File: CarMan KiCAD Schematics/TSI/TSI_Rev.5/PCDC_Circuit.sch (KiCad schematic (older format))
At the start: 57 parts, among them IC1 TS431ILT, J30 GLV Hook-up Pin, K1 APAN3105, Q1 ZVP1320F, Q3 SI1302DL-T1-E3, U10 MC7805BDTRKG, U12 REF3033, U19 SN74HC00APWR, U21 MCP6004, U27 TLP293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

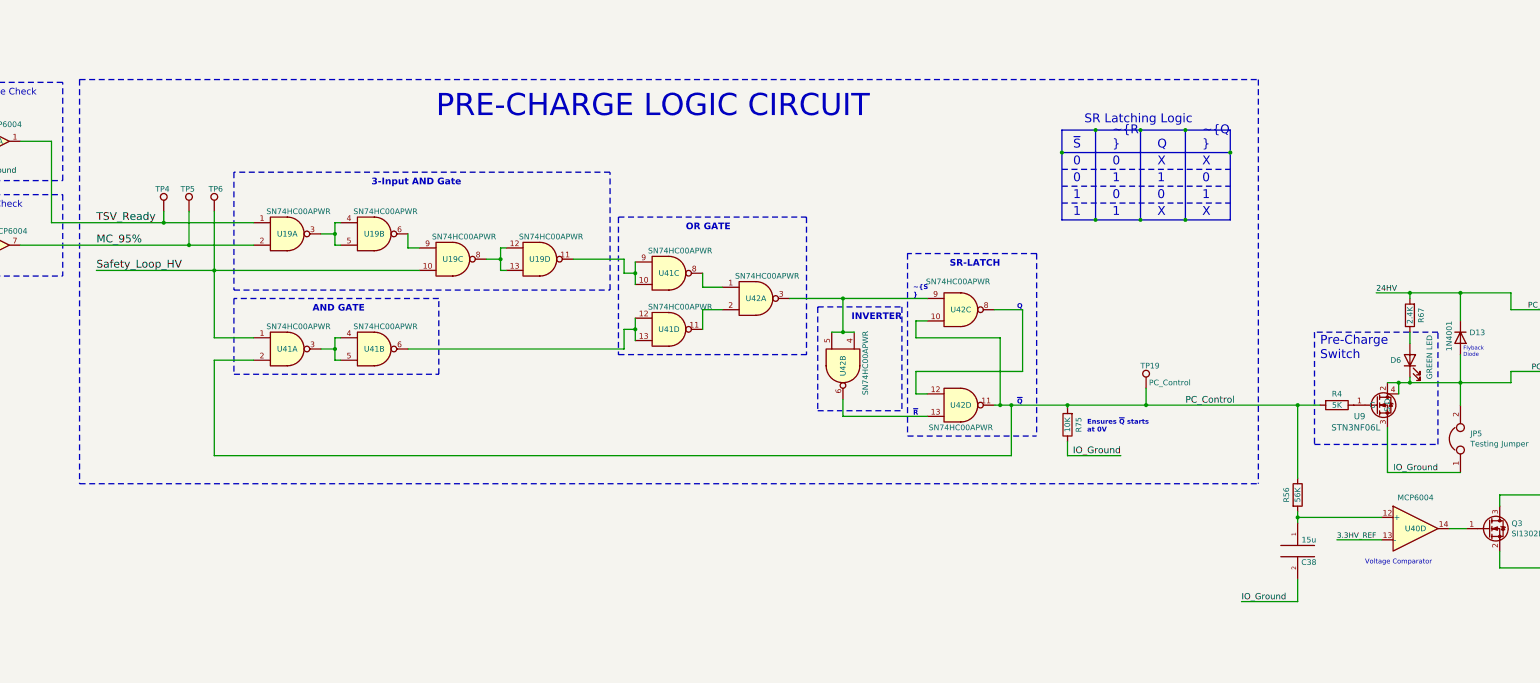
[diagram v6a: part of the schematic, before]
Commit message: Changed D6, Pre-Charge LED to a better circuit, wasn't working before. floating voltage at gate of Xsistor U9 was turning it on always
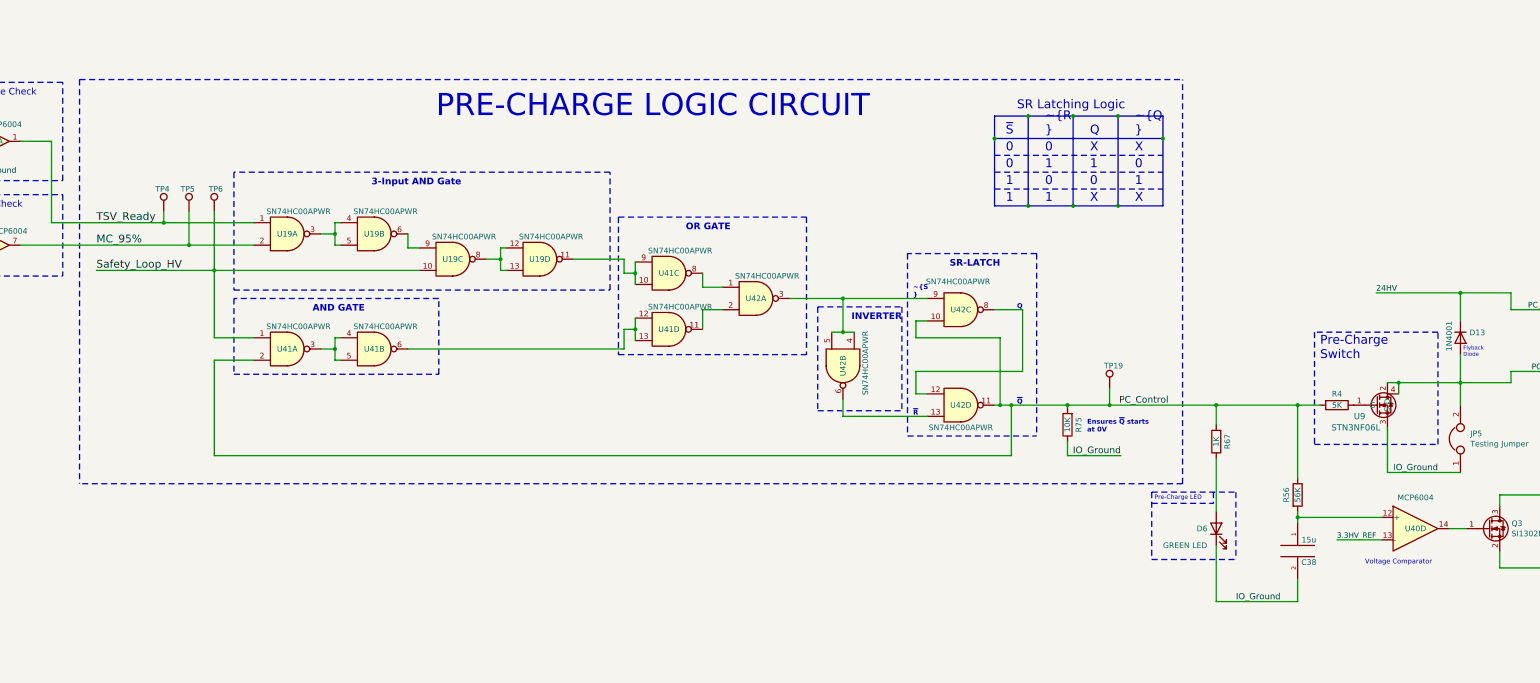
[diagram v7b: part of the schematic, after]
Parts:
- R67: value 2.4K -> 1K
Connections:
- net DC_RELAY-: now also D6.1 (K)
- net PC_Control: now also R67.2
- net PC_RELAY+: no longer R67.2
- net PC_RELAY-: no longer D6.1 (K)
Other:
- note added: "Pre-Charge LED"
- moved on the sheet: D6, R67, TP19
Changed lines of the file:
@@
 Wire Wire Line
 	17050 6425 17050 6625
-Connection ~ 16600 6425
-Wire Wire Line
-	16600 6425 16500 6425
-Wire Wire Line
-	16600 5625 16600 5675
-Wire Wire Line
-	16600 5975 16600 6075
-Wire Wire Line
-	16600 6425 16600 6375
-Wire Wire Line
-	16300 5625 16600 5625
 Text Label 16850 7225 2    55   ~ 0
 IO_Ground
-Connection ~ 16600 5625
 Wire Wire Line
 	16400 7225 17050 7225
@@
 Wire Wire Line
 	17050 5625 17050 5875
-Wire Wire Line
-	16600 6425 17050 6425
-Wire Wire Line
-	16600 5625 17050 5625
 $Comp
 L Device:D D13
@@
 PRE-CHARGE LOGIC CIRCUIT
 Wire Notes Line
-	4750 3725 4750 7325
-Wire Notes Line
 	18075 3600 22100 3600
 Wire Notes Line
@@
 	1    0    0    -1
 $EndComp
-Text Label 15100 8375 0    55   ~ 0
+Text Label 15050 8375 0    55   ~ 0
 IO_Ground
-Wire Wire Line
-	15100 8375 15600 8375
 $Comp
 L Device:LED D6
 U 1 1 5F9CE834
-P 16600 6225
-F 0 "D6" V 16600 6400 50  0000 R CNN
-F 1 "GREEN LED" H 16825 6050 50  0000 R CNN
-F 2 "LED_SMD:LED_0805_2012Metric_Pad1.15x1.40mm_HandSolder" H 16600 6225 50  0001 C CNN
-F 3 "http://static.vcclite.com/pdf/VAOL-S8GT4-LED-0805-green.pdf" H 16600 6225 50  0001 C CNN
-F 4 "VAOL-S8GT4" V 16600 6225 50  0001 C CNN "Part Name"
-	1    16600 6225
+P 14875 7725
+F 0 "D6" V 14875 7900 50  0000 R CNN
+F 1 "GREEN LED" V 14725 8200 50  0000 R CNN
+F 2 "LED_SMD:LED_0805_2012Metric_Pad1.15x1.40mm_HandSolder" H 14875 7725 50  0001 C CNN
+F 3 "http://static.vcclite.com/pdf/VAOL-S8GT4-LED-0805-green.pdf" H 14875 7725 50  0001 C CNN
+F 4 "VAOL-S8GT4" V 14875 7725 50  0001 C CNN "Part Name"
+	1    14875 7725
 	0    -1   -1   0
 $EndComp
-Wire Notes Line
-	4750 3725 15250 3725
-Wire Notes Line
-	4750 7325 15250 7325
-Text Label 14600 6625 0    59   ~ 0
+Text Label 14450 6625 2    59   ~ 0
 PC_Control
-Connection ~ 14250 6625
-Wire Wire Line
-	14250 6625 15600 6625
-Wire Wire Line
-	13550 6625 14250 6625
+Wire Wire Line
+	13550 6625 13925 6625
 $Comp
 L Connector:TestPoint TP?
 U 1 1 60D4CBAD
-P 14250 6475
+P 13925 6475
 AR Path="/5FC85F57/60D4CBAD" Ref="TP?"  Part="1"
 AR Path="/6196BF15/60D4CBAD" Ref="TP19"  Part="1"
-F 0 "TP19" H 14200 6675 50  0000 L CNN
-F 1 "PC_Control" H 14275 6525 50  0000 L CNN
-F 2 "TestPoint:TestPoint_Pad_D3.0mm" H 14450 6475 50  0001 C CNN
-F 3 "~" H 14450 6475 50  0001 C CNN
-	1    14250 6475
-	1    0    0    -1
-$EndComp
-Wire Wire Line
-	14250 6475 14250 6625
-Wire Notes Line
-	15250 3725 15250 7325
-Wire Bus Line
-	15000 4175 15000 4375
-Wire Bus Line
-	13500 4175 13500 4375
-Wire Bus Line
-	15000 4375 15000 4975
-Connection ~ 15000 4375
-Wire Bus Line
-	13500 4375 13500 4975
-Connection ~ 13500 4375
-Text Notes 14750 4650 0    79   ~ 0
+F 0 "TP19" H 13875 6675 50  0000 L CNN
+F 1 "PC_Control" H 13950 6525 50  0001 L CNN
+F 2 "TestPoint:TestPoint_Pad_D3.0mm" H 14125 6475 50  0001 C CNN
+F 3 "~" H 14125 6475 50  0001 C CNN
+	1    13925 6475
+	1    0    0    -1
+$EndComp
+Wire Wire Line
+	13925 6475 13925 6625
+Wire Bus Line
+	14400 4050 14400 4250
+Wire Bus Line
+	12900 4050 12900 4250
+Wire Bus Line
+	14400 4250 14400 4850
+Connection ~ 14400 4250
+Wire Bus Line
+	12900 4250 12900 4850
+Connection ~ 12900 4250
+Text Notes 14150 4525 0    79   ~ 0
 0\n
-Text Notes 14350 4950 0    79   ~ 0
+Text Notes 13750 4825 0    79   ~ 0
 X
-Text Notes 14425 4500 2    79   ~ 0
+Text Notes 13825 4375 2    79   ~ 0
 X
 Wire Notes Line
-	13500 4825 15000 4825
-Wire Notes Line
-	13500 4675 15000 4675
-Wire Notes Line
-	13500 4525 15000 4525
-Wire Bus Line
-	15000 4375 13500 4375
-Wire Bus Line
-	14600 4975 15000 4975
-Wire Bus Line
-	14600 4175 14600 4975
-Connection ~ 14600 4975
-Connection ~ 14600 4175
-Text Notes 14750 4500 0    79   ~ 0
+	12900 4700 14400 4700
+Wire Notes Line
+	12900 4550 14400 4550
+Wire Notes Line
+	12900 4400 14400 4400
+Wire Bus Line
+	14400 4250 12900 4250
+Wire Bus Line
+	14000 4850 14400 4850
+Wire Bus Line
+	14000 4050 14000 4850
+Connection ~ 14000 4850
+Connection ~ 14000 4050
+Text Notes 14150 4375 0    79   ~ 0
 X
-Text Notes 14750 4950 0    79   ~ 0
+Text Notes 14150 4825 0    79   ~ 0
 X
-Text Notes 14750 4800 0    79   ~ 0
+Text Notes 14150 4675 0    79   ~ 0
 1
 Wire Bus Line
-	15000 4175 14600 4175
-Text Notes 14750 4350 0    79   ~ 0
+	14400 4050 14000 4050
+Text Notes 14150 4225 0    79   ~ 0
 ~Q\n
-Text Notes 13700 4125 0    79   ~ 0
+Text Notes 13100 4000 0    79   ~ 0
 SR Latching Logic\n
 Wire Bus Line
-	14200 4975 14600 4975
-Wire Bus Line
-	14200 4175 14200 4975
-Connection ~ 14200 4975
-Text Notes 14350 4800 0    79   ~ 0
+	13600 4850 14000 4850
+Wire Bus Line
+	13600 4050 13600 4850
+Connection ~ 13600 4850
+Text Notes 13750 4675 0    79   ~ 0
 0
-Text Notes 14350 4650 0    79   ~ 0
+Text Notes 13750 4525 0    79   ~ 0
 1\n
-Text Notes 13950 4650 0    79   ~ 0
+Text Notes 13350 4525 0    79   ~ 0
 1\n
-Text Notes 13600 4950 0    79   ~ 0
+Text Notes 13000 4825 0    79   ~ 0
 1\n
-Text Notes 13600 4800 0    79   ~ 0
+Text Notes 13000 4675 0    79   ~ 0
 1\n
-Text Notes 13950 4950 0    79   ~ 0
+Text Notes 13350 4825 0    79   ~ 0
 1\n
-Text Notes 13950 4500 0    79   ~ 0
+Text Notes 13350 4375 0    79   ~ 0
 0
-Text Notes 13950 4800 0    79   ~ 0
+Text Notes 13350 4675 0    79   ~ 0
 0
-Text Notes 13600 4650 0    79   ~ 0
+Text Notes 13000 4525 0    79   ~ 0
 0
-Text Notes 13600 4500 0    79   ~ 0
+Text Notes 13000 4375 0    79   ~ 0
 0
 Wire Bus Line
-	14200 4175 13800 4175
-Connection ~ 14200 4175
-Wire Bus Line
-	13800 4975 14200 4975
-Connection ~ 13800 4975
-Wire Bus Line
-	13800 4175 13500 4175
-Connection ~ 13800 4175
-Wire Bus Line
-	13800 4175 13800 4975
-Wire Bus Line
-	13500 4975 13800 4975
-Wire Bus Line
-	14600 4175 14200 4175
-Text Notes 14350 4350 0    79   ~ 0
+	13600 4050 13200 4050
+Connection ~ 13600 4050
+Wire Bus Line
+	13200 4850 13600 4850
+Connection ~ 13200 4850
+Wire Bus Line
+	13200 4050 12900 4050
+Connection ~ 13200 4050
+Wire Bus Line
+	13200 4050 13200 4850
+Wire Bus Line
+	12900 4850 13200 4850
+Wire Bus Line
+	14000 4050 13600 4050
+Text Notes 13750 4225 0    79   ~ 0
 Q\n
-Text Notes 13950 4350 0    79   ~ 0
+Text Notes 13350 4225 0    79   ~ 0
 ~R\n
-Text Notes 13600 4350 0    79   ~ 0
+Text Notes 13000 4225 0    79   ~ 0
 ~S
 $Comp
 L Device:R R67
 U 1 1 5F9DBFC0
-P 16600 5825
-F 0 "R67" V 16500 5825 50  0000 C CNN
-F 1 "2.4K" V 16600 5825 50  0000 C CNN
-F 2 "Resistor_SMD:R_0805_2012Metric_Pad1.15x1.40mm_HandSolder" V 16530 5825 50  0001 C CNN
-F 3 "~" H 16600 5825 50  0001 C CNN
-	1    16600 5825
+P 14875 6950
+F 0 "R67" V 14775 6950 50  0000 C CNN
+F 1 "1K" V 14875 6950 50  0000 C CNN
+F 2 "Resistor_SMD:R_0805_2012Metric_Pad1.15x1.40mm_HandSolder" V 14805 6950 50  0001 C CNN
+F 3 "~" H 14875 6950 50  0001 C CNN
+	1    14875 6950
 	-1   0    0    1
 $EndComp
 Text Label 8720 12025 2    50   ~ 0
 IO_Ground
+Connection ~ 13925 6625
+Wire Wire Line
+	13925 6625 14875 6625
+Wire Notes Line
+	14575 7325 4750 7325
+Wire Notes Line
+	4750 3725 4750 7325
+Wire Wire Line
+	16300 5625 17050 5625
+Wire Wire Line
+	16500 6425 17050 6425
+Wire Wire Line
+	14875 6625 14875 6800
+Connection ~ 14875 6625
+Wire Wire Line
+	14875 6625 15600 6625
+Wire Wire Line
+	14875 8375 15600 8375
+Wire Wire Line
+	14875 7875 14875 8375
+Wire Wire Line
+	14875 7100 14875 7575
+Text Notes 14325 7475 0    39   ~ 0
+Pre-Charge LED
+Wire Notes Line
+	14300 7400 15050 7400
+Wire Notes Line
+	14850 7400 14850 7500
+Wire Notes Line
+	14575 7325 14575 3725
+Wire Notes Line
+	4750 3725 14575 3725
+Wire Notes Line
+	14300 7500 14850 7500
+Wire Notes Line
+	15050 7400 15050 8000
+Wire Notes Line
+	14300 8000 15050 8000
+Wire Notes Line
+	14300 7400 14300 8000
 $EndSCHEMATC

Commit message: changed the "speical" footprint of U9 to the correct one
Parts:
- U9: footprint TSI_Rev_2021_Footprint_Lib:SOT230P700X180-4N-speical -> TSI_Rev_2021_Footprint_Lib:SOT230P700X180-4N
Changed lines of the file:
@@
 F 0 "U9" H 16100 6525 55  0000 L CNN
 F 1 "STN3NF06L" H 15900 6425 55  0000 L CNN
-F 2 "TSI_Rev_2021_Footprint_Lib:SOT230P700X180-4N-speical" H 15950 6975 55  0001 C CNN
+F 2 "TSI_Rev_2021_Footprint_Lib:SOT230P700X180-4N" H 15950 6975 55  0001 C CNN
 F 3 "https://www.st.com/content/ccc/resource/technical/document/datasheet/b1/52/93/f0/a9/a9/40/d7/CD00002430.pdf/files/CD00002430.pdf/jcr:content/translations/en.CD00002430.pdf" H 15950 6975 55  0001 C CNN
 	1    16350 6625
